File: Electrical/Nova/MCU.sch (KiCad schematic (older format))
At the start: 1 part, among them U201 STM32F401RBTx

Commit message: Added Barometer, Flash, SD, and Power Supply
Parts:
- U201: symbol Nova_Microcontroller:STM32F401RBTx -> Nova-rescue:STM32F401RBTx-Nova_Microcontroller
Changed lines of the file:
@@
 $Descr A4 11693 8268
 encoding utf-8
-Sheet 9 9
+Sheet 9 13
 Title "Microcontroller"
 Date "2020-07-02"
@@
 	5000 2200 5350 2200
 $Comp
-L Nova_Microcontroller:STM32F401RBTx U201
+L Nova-rescue:STM32F401RBTx-Nova_Microcontroller U201
 U 1 1 5EE690AA
 P 6050 3700

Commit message: Fixed Power Supply
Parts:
- U201: symbol Nova-rescue:STM32F401RBTx-Nova_Microcontroller -> Nova-rescue:STM32F401RBTx-Nova_Microcontroller-Nova-rescue
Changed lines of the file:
@@
 	5000 2200 5350 2200
 $Comp
-L Nova-rescue:STM32F401RBTx-Nova_Microcontroller U201
+L Nova-rescue:STM32F401RBTx-Nova_Microcontroller-Nova-rescue U201
 U 1 1 5EE690AA
 P 6050 3700

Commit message: Work from 8/17/20 Meeting
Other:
- note added: "Accelerometer\n"
- note added: "Barometer"
- note added: "Gyro"
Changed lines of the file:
@@
 $Descr A4 11693 8268
 encoding utf-8
-Sheet 9 13
+Sheet 13 13
 Title "Microcontroller"
 Date "2020-07-02"
@@
 EndData
 $EndBitmap
+Text Notes 7450 3900 0    50   ~ 0
+Barometer
+Text Notes 7450 4000 0    50   ~ 0
+Accelerometer\n
+Text Notes 7450 4100 0    50   ~ 0
+Gyro
 $EndSCHEMATC

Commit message: Added Gyroscope
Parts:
- U201: symbol Nova-rescue:STM32F401RBTx-Nova_Microcontroller-Nova-rescue -> Nova-rescue:STM32F401RBTx-Nova_Microcontroller-Nova-rescue-Nova-rescue
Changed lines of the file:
@@
 $Descr A4 11693 8268
 encoding utf-8
-Sheet 13 13
+Sheet 13 14
 Title "Microcontroller"
 Date "2020-07-02"
@@
 	5000 2200 5350 2200
 $Comp
-L Nova-rescue:STM32F401RBTx-Nova_Microcontroller-Nova-rescue U201
+L Nova-rescue:STM32F401RBTx-Nova_Microcontroller-Nova-rescue-Nova-rescue U201
 U 1 1 5EE690AA
 P 6050 3700

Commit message: Added Gyro pins. Organized Schematic
Need to determine if we need the interrupt pins for the sensors.
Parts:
- U201: symbol Nova-rescue:STM32F401RBTx-Nova_Microcontroller-Nova-rescue-Nova-rescue -> Nova-rescue:STM32F401RBTx-Nova_Microcontroller-Nova-rescue-Nova-rescue-Nova-rescue
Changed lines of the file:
@@
 	5000 2200 5350 2200
 $Comp
-L Nova-rescue:STM32F401RBTx-Nova_Microcontroller-Nova-rescue-Nova-rescue U201
+L Nova-rescue:STM32F401RBTx-Nova_Microcontroller-Nova-rescue-Nova-rescue-Nova-rescue U201
 U 1 1 5EE690AA
 P 6050 3700

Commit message: Added Pyro Channels
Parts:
- U201: symbol Nova-rescue:STM32F401RBTx-Nova_Microcontroller-Nova-rescue-Nova-rescue-Nova-rescue -> Nova-rescue:STM32F401RBTx-Nova_Microcontroller-Nova-rescue-Nova-rescue-Nova-rescue-Nova-rescue
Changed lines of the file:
@@
 $Descr A4 11693 8268
 encoding utf-8
-Sheet 13 14
+Sheet 13 16
 Title "Microcontroller"
 Date "2020-07-02"
@@
 	5000 2200 5350 2200
 $Comp
-L Nova-rescue:STM32F401RBTx-Nova_Microcontroller-Nova-rescue-Nova-rescue-Nova-rescue U201
+L Nova-rescue:STM32F401RBTx-Nova_Microcontroller-Nova-rescue-Nova-rescue-Nova-rescue-Nova-rescue U201
 U 1 1 5EE690AA
 P 6050 3700

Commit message: Added LED sheet and pins
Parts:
- U201: symbol Nova-rescue:STM32F401RBTx-Nova_Microcontroller-Nova-rescue-Nova-rescue-Nova-rescue-Nova-rescue -> Nova-rescue:STM32F401RBTx-Nova_Microcontroller-Nova-rescue-Nova-rescue-Nova-rescue-Nova-rescue-Nova-rescue
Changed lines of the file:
@@
 $Descr A4 11693 8268
 encoding utf-8
-Sheet 13 16
+Sheet 13 18
 Title "Microcontroller"
 Date "2020-07-02"
@@
 	5000 2200 5350 2200
 $Comp
-L Nova-rescue:STM32F401RBTx-Nova_Microcontroller-Nova-rescue-Nova-rescue-Nova-rescue-Nova-rescue U201
+L Nova-rescue:STM32F401RBTx-Nova_Microcontroller-Nova-rescue-Nova-rescue-Nova-rescue-Nova-rescue-Nova-rescue U201
 U 1 1 5EE690AA
 P 6050 3700

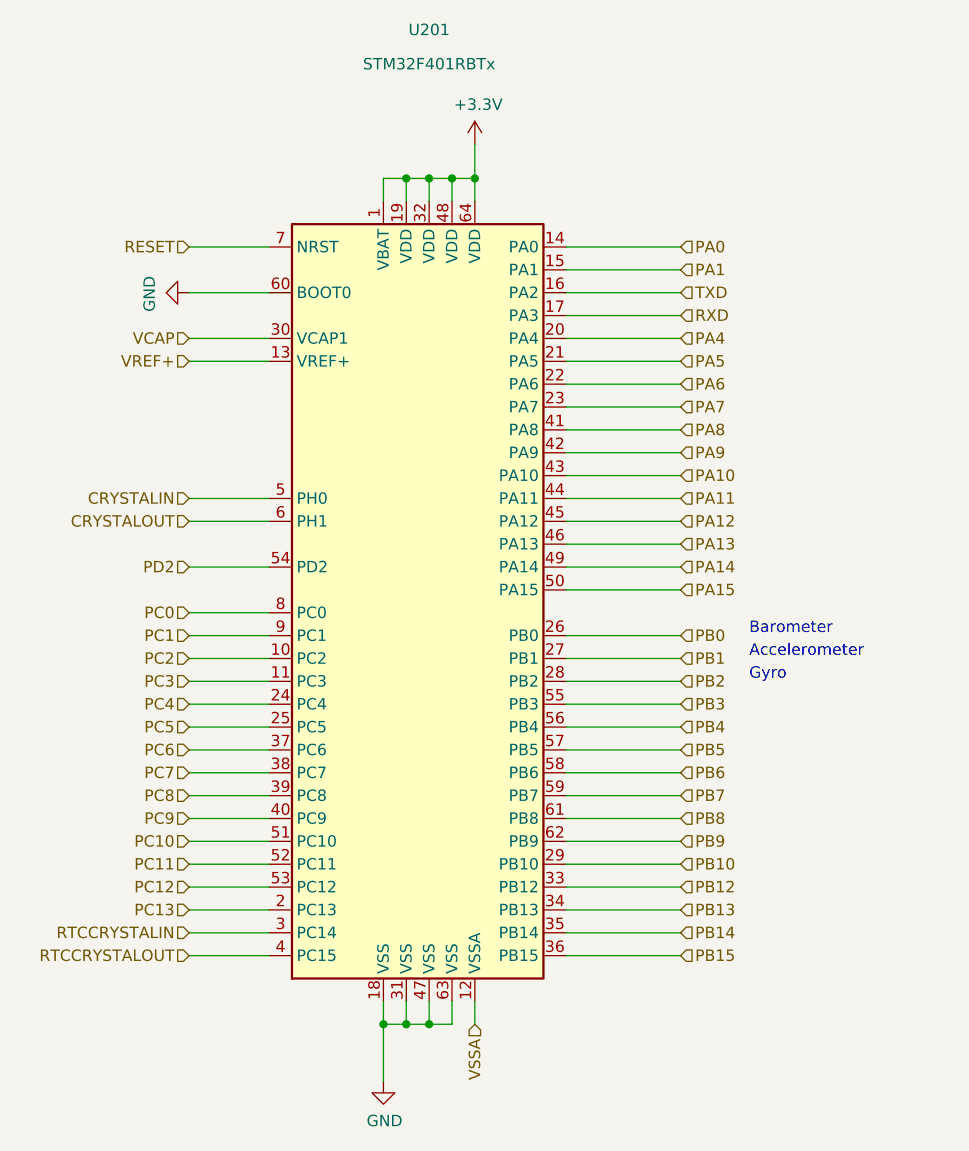
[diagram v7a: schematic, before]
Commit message: Finished CS Pin Selection
Still need High-G accelerometer pushed
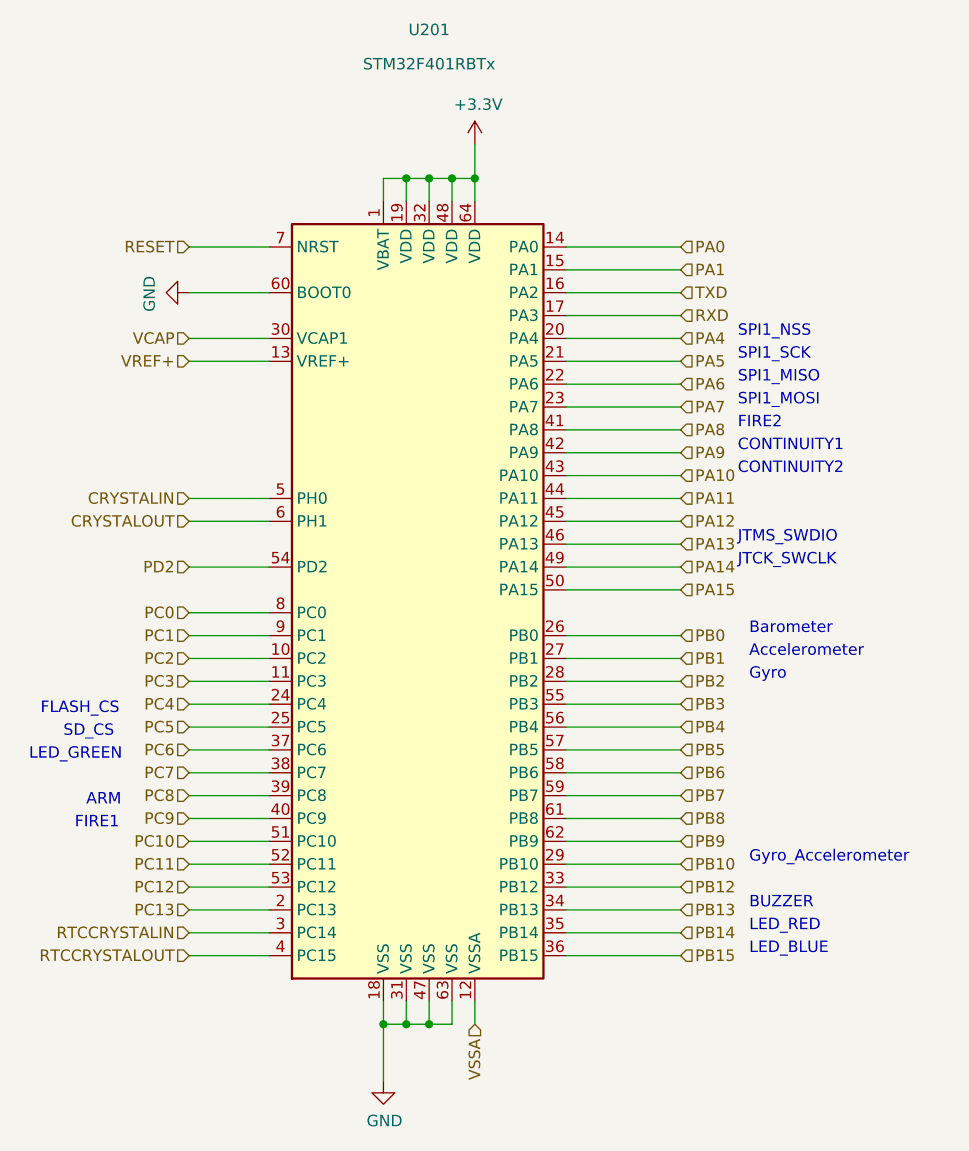
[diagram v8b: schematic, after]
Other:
- note added: "ARM\n"
- note added: "BUZZER"
- note added: "CONTINUITY1"
- note added: "CONTINUITY2"
- note added: "FIRE1\n"
- note added: "FIRE2"
- note added: "FLASH_CS\n"
- note added: "Gyro_Accelerometer\n"
- note added: "JTCK_SWCLK"
- note added: "JTMS_SWDIO"
- note added: "LED_BLUE\n"
- note added: "LED_GREEN\n"
- note added: "LED_RED\n"
- note added: "SD_CS\n"
- note added: "SPI1_MISO\n"
- note added: "SPI1_MOSI"
- note added: "SPI1_NSS\n"
- note added: "SPI1_SCK\n"
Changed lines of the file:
@@
 $Descr A4 11693 8268
 encoding utf-8
-Sheet 13 18
+Sheet 12 18
 Title "Microcontroller"
 Date "2020-07-02"
@@
 Text Notes 7450 4100 0    50   ~ 0
 Gyro
+Text Notes 7450 4900 0    50   ~ 0
+Gyro_Accelerometer\n
+Text Notes 4350 4250 0    50   ~ 0
+FLASH_CS\n
+Text Notes 4450 4350 0    50   ~ 0
+SD_CS\n
+Text Notes 7450 5100 0    50   ~ 0
+BUZZER
+Text Notes 7450 5200 0    50   ~ 0
+LED_RED\n
+Text Notes 7450 5300 0    50   ~ 0
+LED_BLUE\n
+Text Notes 4300 4450 0    50   ~ 0
+LED_GREEN\n
+Text Notes 4550 4650 0    50   ~ 0
+ARM\n
+Text Notes 4500 4750 0    50   ~ 0
+FIRE1\n
+Text Notes 7400 3000 0    50   ~ 0
+FIRE2
+Text Notes 7400 3100 0    50   ~ 0
+CONTINUITY1
+Text Notes 7400 3200 0    50   ~ 0
+CONTINUITY2
+Text Notes 7400 2600 0    50   ~ 0
+SPI1_NSS\n
+Text Notes 7400 2700 0    50   ~ 0
+SPI1_SCK\n
+Text Notes 7400 2800 0    50   ~ 0
+SPI1_MISO\n
+Text Notes 7400 2900 0    50   ~ 0
+SPI1_MOSI
+Text Notes 7400 3500 0    50   ~ 0
+JTMS_SWDIO
+Text Notes 7400 3600 0    50   ~ 0
+JTCK_SWCLK
 $EndSCHEMATC
